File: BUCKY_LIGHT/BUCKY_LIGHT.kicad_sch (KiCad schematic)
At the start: 170 parts, among them Q1 Q_Photo_NPN, Q10 Q_Photo_NPN, Q11 Q_Photo_NPN, Q12 Q_Photo_NPN, Q13 Q_Photo_NPN, Q14 Q_Photo_NPN, Q15 Q_Photo_NPN, Q16 Q_Photo_NPN, Q17 Q_Photo_NPN, Q18 Q_Photo_NPN, Q19 Q_Photo_NPN, Q2 Q_Photo_NPN, Q20 Q_Photo_NPN, Q21 Q_Photo_NPN, Q22 Q_Photo_NPN, Q23 Q_Photo_NPN, Q24 Q_Photo_NPN, Q25 Q_Photo_NPN, Q26 Q_Photo_NPN, Q27 Q_Photo_NPN, Q28 Q_Photo_NPN, Q29 Q_Photo_NPN, Q3 Q_Photo_NPN, Q30 Q_Photo_NPN, Q31 Q_Photo_NPN, Q32 Q_Photo_NPN, Q4 Q_Photo_NPN, Q5 Q_Photo_NPN, Q6 Q_Photo_NPN, Q7 Q_Photo_NPN, Q8 Q_Photo_NPN, Q9 Q_Photo_NPN, U1 FRONT, U2 RIGHT, U3 DOWN, U4 LEFT

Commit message: Started Light PCB
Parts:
- removed C29, C30, C31, C32: 0.1u, Capacitor_SMD:C_0603_1608Metric_Pad1.08x0.95mm_HandSolder, symbol Device:C
- removed D29, D30, D31, D32: LED, LED_SMD:LED_0603_1608Metric, symbol Device:LED
- removed Q29, Q30, Q31, Q32: Q_Photo_NPN, Light_Ring:XDCR_ALS-PT19-315C_L177_TR8, symbol Device:Q_Photo_NPN
- removed R57, R58, R59, R60: 10k, Resistor_SMD:R_0603_1608Metric_Pad0.98x0.95mm_HandSolder, symbol Device:R
- removed R61, R62, R63, R64: 12R, Resistor_SMD:R_0603_1608Metric_Pad0.98x0.95mm_HandSolder, symbol Device:R
- C1, C10, C11, C12, C13, C14, C15, C16, C17, C18, C19, C2, C20, C21, C22, C23, C24, C25, C26, C27, C28, C3, C4, C5, C6, C7, C8, C9: footprint Capacitor_SMD:C_0603_1608Metric_Pad1.08x0.95mm_HandSolder -> Capacitor_SMD:C_0805_2012Metric_Pad1.18x1.45mm_HandSolder
- D1, D10, D11, D12, D13, D14, D15, D16, D17, D18, D19, D2, D20, D21, D22, D23, D24, D25, D26, D27, D28, D3, D4, D5, D6, D7, D8, D9: footprint LED_SMD:LED_0603_1608Metric -> LED_SMD:LED_PLCC-2
- J1: renamed from J?; footprint (none) -> Connector_JST:JST_PH_B6B-PH-SM4-TB_1x06-1MP_P2.00mm_Vertical
- J2: renamed from J?; footprint (none) -> Connector_JST:JST_PH_S6B-PH-SM4-TB_1x06-1MP_P2.00mm_Horizontal
- Q1, Q10, Q11, Q12, Q13, Q14, Q15, Q16, Q17, Q18, Q19, Q2, Q20, Q21, Q22, Q23, Q24, Q25, Q26, Q27, Q28, Q3, Q4, Q5, Q6, Q7, Q8, Q9: footprint Light_Ring:XDCR_ALS-PT19-315C_L177_TR8 -> BUCKY_LIGHT:XDCR_ALS-PT19-315C_L177_TR8
- R1, R10, R11, R12, R17, R18, R19, R2, R20, R25, R26, R27, R28, R3, R33, R34, R35, R36, R4, R41, R42, R43, R44, R49, R50, R51, R52, R9: footprint Resistor_SMD:R_0603_1608Metric_Pad0.98x0.95mm_HandSolder -> Resistor_SMD:R_0603_1608Metric
- R13, R14, R15, R16, R21, R22, R23, R24, R29, R30, R31, R32, R37, R38, R39, R40, R45, R46, R47, R48, R5, R53, R54, R55, R56, R6, R7, R8: value 12R -> 90R; footprint Resistor_SMD:R_0603_1608Metric_Pad0.98x0.95mm_HandSolder -> Resistor_SMD:R_0603_1608Metric
- R65, R66: renamed from R?; footprint (none) -> Resistor_SMD:R_0805_2012Metric_Pad1.20x1.40mm_HandSolder
- U1, U2, U3, U4: footprint (none) -> Package_SO:SOIC-16_3.9x9.9mm_P1.27mm
- U6: renamed from U?; value ESP32-WROOM-32D -> ESP32-WROOM-32U; footprint RF_Module:ESP32-WROOM-32 -> RF_Module:ESP32-WROOM-32U; symbol RF_Module:ESP32-WROOM-32D -> RF_Module:ESP32-WROOM-32U
- gave numbers to parts that had none: 1
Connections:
- net L29 is gone; now on net L26: U1.13 (A0)
- net L30 is gone; now on net L27: U1.14 (A1)
- net L31 is gone; now on net L28: U1.15 (A2)
- net L32 is gone; now on net L1: U1.12 (A3)
- net L1: no longer U1.1 (A4)
- net L12: now also U3.13 (A0); no longer U2.4 (A7)
- net L13: now also U3.14 (A1); no longer U3.13 (A0)
- net L14: now also U3.15 (A2); no longer U3.14 (A1)
- net L15: now also U3.12 (A3); no longer U3.15 (A2)
- net L16: now also U3.1 (A4); no longer U3.12 (A3)
- net L17: now also U3.5 (A5); no longer U3.1 (A4)
- net L18: now also U3.2 (A6); no longer U3.5 (A5)
- net L19: now also U4.13 (A0); no longer U3.2 (A6)
- net L2: now also U1.1 (A4); no longer U1.5 (A5)
- net L20: now also U4.14 (A1); no longer U3.4 (A7)
- net L21: now also U4.15 (A2); no longer U4.13 (A0)
- net L22: now also U4.12 (A3); no longer U4.14 (A1)
- net L23: now also U4.1 (A4); no longer U4.15 (A2)
- net L24: now also U4.5 (A5); no longer U4.12 (A3)
- net L25: now also U4.2 (A6); no longer U4.1 (A4)
- net L26: no longer U4.5 (A5)
- net L27: no longer U4.2 (A6)
- net L28: no longer U4.4 (A7)
- net L3: now also U1.5 (A5); no longer U1.2 (A6)
- net L4: now also U1.2 (A6); no longer U1.4 (A7)
- no-connect marks 12 -> 16
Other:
- note added: "IF Vf = 3.1V, then Rled = 90R IF Vf = 2.9V, then Rled = 25R"
- note removed: "IF Vf = 3.1V, then Rled = 12R IF Vf = 2.9V, then Rled = 25R"

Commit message: Some LIGHT dev
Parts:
- removed C10, C11, C12, C13, C14, C15, C16, C17, C18, C19, C20, C21, C22, C23, C24, C25, C26, C27, C28, C5, C6, C7, C8, C9: 0.1u, Capacitor_SMD:C_0805_2012Metric_Pad1.18x1.45mm_HandSolder, symbol Device:C
- added U7: AMS1117-3.3, Package_TO_SOT_SMD:SOT-223-3_TabPin2, symbol Regulator_Linear:AMS1117-3.3
- C1: value 0.1u -> 22u; footprint Capacitor_SMD:C_0805_2012Metric_Pad1.18x1.45mm_HandSolder -> Capacitor_SMD:C_1210_3225Metric_Pad1.33x2.70mm_HandSolder
- C2, C4: footprint Capacitor_SMD:C_0805_2012Metric_Pad1.18x1.45mm_HandSolder -> Capacitor_SMD:C_1210_3225Metric_Pad1.33x2.70mm_HandSolder
- C3: value 0.1u -> 10u; footprint Capacitor_SMD:C_0805_2012Metric_Pad1.18x1.45mm_HandSolder -> Capacitor_SMD:C_1210_3225Metric_Pad1.33x2.70mm_HandSolder
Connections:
- net +3V3: now also C3.1, C4.1, U7.2 (VO); no longer R13.1, R14.1, R15.1, R16.1, R21.1, R22.1, R23.1, R24.1, R29.1, R30.1, R31.1, R32.1, R37.1, R38.1, R39.1, R40.1, R45.1, R46.1, R47.1, R48.1, R5.1, R53.1, R54.1, R55.1, R56.1, R6.1, R7.1, R8.1
- net +5V: now also C1.1, C2.1, R13.1, R14.1, R15.1, R16.1, R21.1, R22.1, R23.1, R24.1, R29.1, R30.1, R31.1, R32.1, R37.1, R38.1, R39.1, R40.1, R45.1, R46.1, R47.1, R48.1, R5.1, R53.1, R54.1, R6.1, R7.1, R8.1, U7.3 (VI)
- net GND: now also U7.1 (GND)
- net L1: no longer C1.1
- net L2: no longer C2.1
- net L3: no longer C3.1
- net L4: no longer C4.1

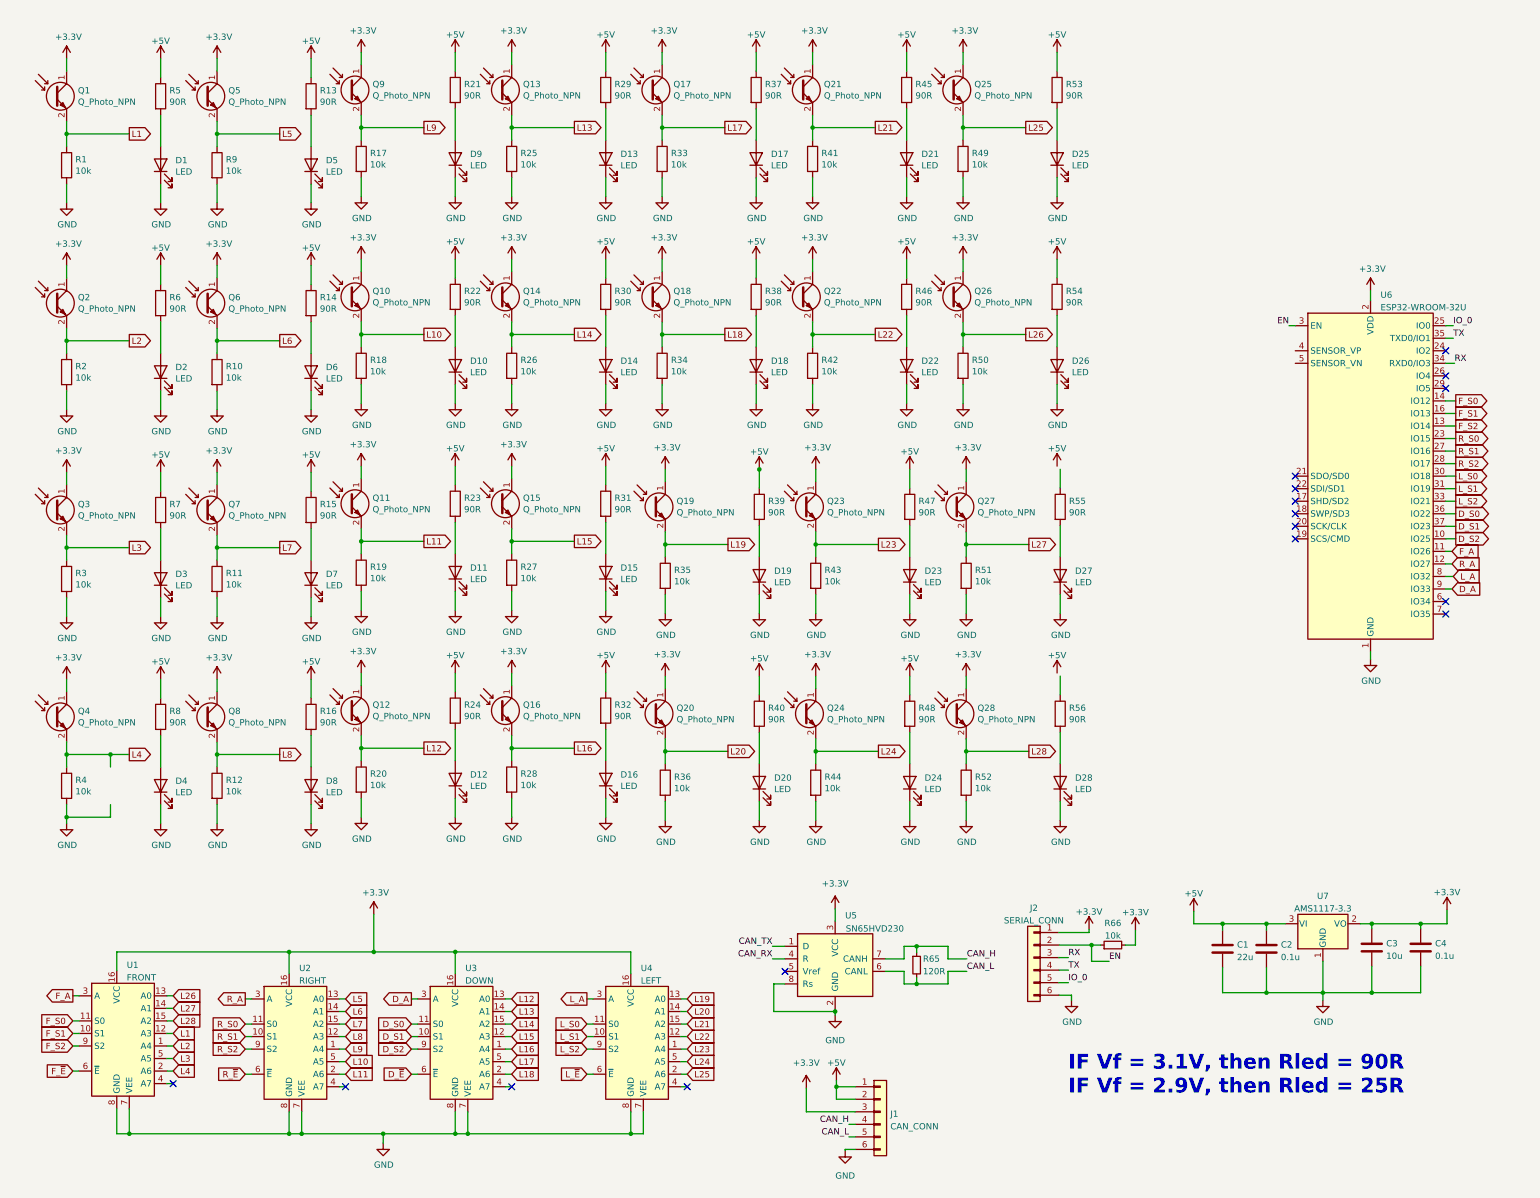
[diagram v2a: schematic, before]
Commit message: Finished bulk of LIGHT, only REF left
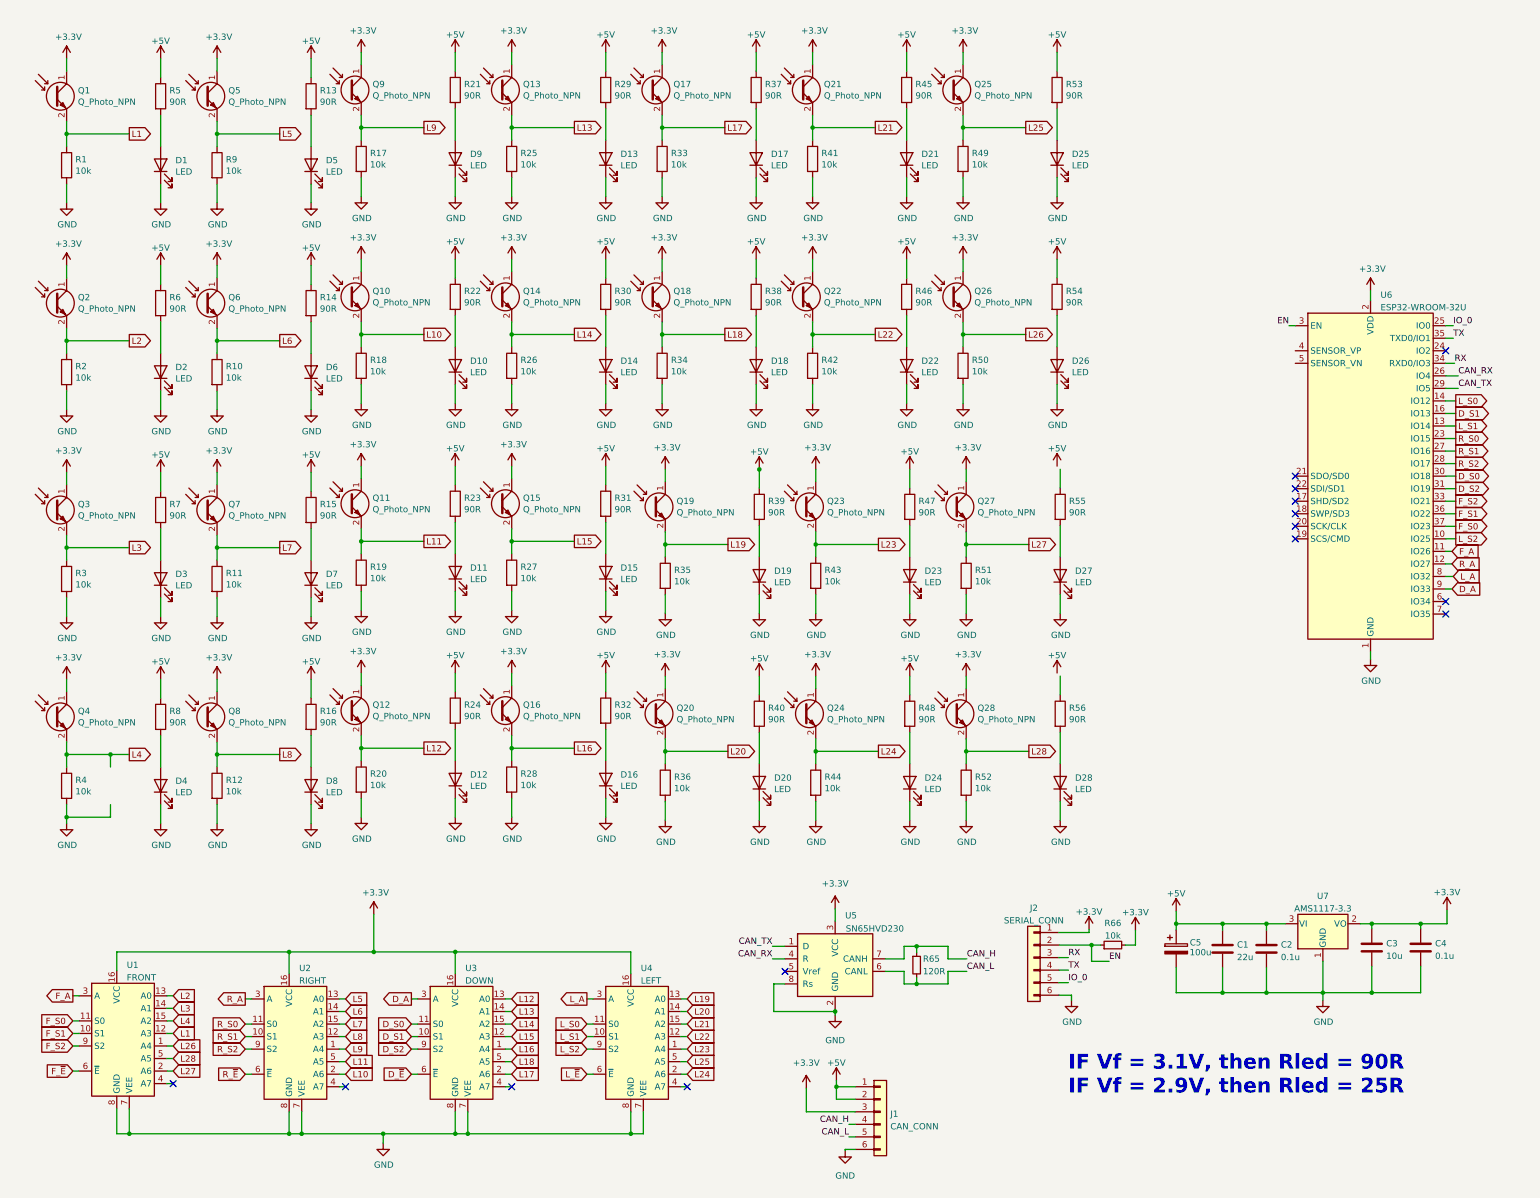
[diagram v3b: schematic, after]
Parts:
- added C5: 100u, Capacitor_SMD:CP_Elec_6.3x7.7, symbol Device:C_Polarized
- C2, C4: footprint Capacitor_SMD:C_1210_3225Metric_Pad1.33x2.70mm_HandSolder -> Capacitor_SMD:C_0603_1608Metric
- J2: footprint Connector_JST:JST_PH_S6B-PH-SM4-TB_1x06-1MP_P2.00mm_Horizontal -> Connector_JST:JST_PH_B6B-PH-SM4-TB_1x06-1MP_P2.00mm_Vertical
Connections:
- net +5V: now also C5.1
- net CAN_RX: now also U6.26 (IO4)
- net CAN_TX: now also U6.29 (IO5)
- net D_S0: now also U6.30 (IO18); no longer U6.36 (IO22)
- net D_S1: now also U6.16 (IO13); no longer U6.37 (IO23)
- net D_S2: now also U6.31 (IO19); no longer U6.10 (IO25)
- net F_S0: now also U6.37 (IO23); no longer U6.14 (IO12)
- net F_S1: now also U6.36 (IO22); no longer U6.16 (IO13)
- net F_S2: now also U6.33 (IO21); no longer U6.13 (IO14)
- net GND: now also C5.2
- net L10: now also U2.2 (A6); no longer U2.5 (A5)
- net L11: now also U2.5 (A5); no longer U2.2 (A6)
- net L17: now also U3.2 (A6); no longer U3.5 (A5)
- net L18: now also U3.5 (A5); no longer U3.2 (A6)
- net L2: now also U1.13 (A0); no longer U1.1 (A4)
- net L24: now also U4.2 (A6); no longer U4.5 (A5)
- net L25: now also U4.5 (A5); no longer U4.2 (A6)
- net L26: now also U1.1 (A4); no longer U1.13 (A0)
- net L27: now also U1.2 (A6); no longer U1.14 (A1)
- net L28: now also U1.5 (A5); no longer U1.15 (A2)
- net L3: now also U1.14 (A1); no longer U1.5 (A5)
- net L4: now also U1.15 (A2); no longer U1.2 (A6)
- net L_S0: now also U6.14 (IO12); no longer U6.30 (IO18)
- net L_S1: now also U6.13 (IO14); no longer U6.31 (IO19)
- net L_S2: now also U6.10 (IO25); no longer U6.33 (IO21)
- no-connect marks 16 -> 14

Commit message: Started POWER
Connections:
- net +5V: now also R55.1, R56.1
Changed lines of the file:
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@@
     (pin "2")
   )
-  (symbol (lib_id "power:+5V") (at 222.25 143.51 0) (unit 1)
-    (in_bom yes) (on_board yes) (fields_autoplaced)
-    (property "Reference" "#PWR0111" (id 0) (at 222.25 147.32 0)
-      (effects (font (size 1.27 1.27)) hide)
-    )
-    (property "Value" "+5V" (id 1) (at 222.25 139.9342 0))
-    (property "Footprint" "" (id 2) (at 222.25 143.51 0)
-      (effects (font (size 1.27 1.27)) hide)
-    )
-    (property "Datasheet" "" (id 3) (at 222.25 143.51 0)
+  (symbol (lib_id "power:+5V") (at 222.885 144.145 0) (unit 1)
+    (in_bom yes) (on_board yes) (fields_autoplaced)
+    (property "Reference" "#PWR0111" (id 0) (at 222.885 147.955 0)
+      (effects (font (size 1.27 1.27)) hide)
+    )
+    (property "Value" "+5V" (id 1) (at 222.885 140.5692 0))
+    (property "Footprint" "" (id 2) (at 222.885 144.145 0)
+      (effects (font (size 1.27 1.27)) hide)
+    )
+    (property "Datasheet" "" (id 3) (at 222.885 144.145 0)
       (effects (font (size 1.27 1.27)) hide)
     )
@@
     (pin "2")
   )
-  (symbol (lib_id "power:+5V") (at 222.25 101.6 0) (unit 1)
-    (in_bom yes) (on_board yes) (fields_autoplaced)
-    (property "Reference" "#PWR0153" (id 0) (at 222.25 105.41 0)
-      (effects (font (size 1.27 1.27)) hide)
-    )
-    (property "Value" "+5V" (id 1) (at 222.25 98.0242 0))
-    (property "Footprint" "" (id 2) (at 222.25 101.6 0)
-      (effects (font (size 1.27 1.27)) hide)
-    )
-    (property "Datasheet" "" (id 3) (at 222.25 101.6 0)
-      (effects (font (size 1.27 1.27)) hide)
-    )
+  (symbol (lib_id "power:+5V") (at 222.885 102.235 0) (unit 1)
+    (in_bom yes) (on_board yes) (fields_autoplaced)
+    (property "Reference" "#PWR0153" (id 0) (at 222.885 106.045 0)
+      (effects (font (size 1.27 1.27)) hide)
+    )
+    (property "Value" "+5V" (id 1) (at 222.885 98.6592 0))
+    (property "Footprint" "" (id 2) (at 222.885 102.235 0)
+      (effects (font (size 1.27 1.27)) hide)
+    )
+    (property "Datasheet" "" (id 3) (at 222.885 102.235 0)
+      (effects (font (size 1.27 1.27)) hide)
+    )

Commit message: chore: start on schematics
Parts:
- removed C1: 22u, Capacitor_SMD:C_1210_3225Metric_Pad1.33x2.70mm_HandSolder, symbol Device:C
- removed C2, C4: 0.1u, Capacitor_SMD:C_0603_1608Metric, symbol Device:C
- removed C3: 10u, Capacitor_SMD:C_1210_3225Metric_Pad1.33x2.70mm_HandSolder, symbol Device:C
- removed C5: 100u, Capacitor_SMD:CP_Elec_6.3x7.7, symbol Device:C_Polarized
- removed J1: CAN_CONN, Connector_JST:JST_PH_B6B-PH-SM4-TB_1x06-1MP_P2.00mm_Vertical, symbol Connector_Generic:Conn_01x06
- removed J2: SERIAL_CONN, Connector_JST:JST_PH_B6B-PH-SM4-TB_1x06-1MP_P2.00mm_Vertical, symbol Connector_Generic:Conn_01x06
- removed R65: 120R, Resistor_SMD:R_0805_2012Metric_Pad1.20x1.40mm_HandSolder, symbol Device:R_Small
- removed R66: 10k, Resistor_SMD:R_0805_2012Metric_Pad1.20x1.40mm_HandSolder, symbol Device:R_Small
- removed U5: SN65HVD230, Package_SO:SOIC-8_3.9x4.9mm_P1.27mm, symbol Interface_CAN_LIN:SN65HVD230
- removed U6: ESP32-WROOM-32U, RF_Module:ESP32-WROOM-32U, symbol RF_Module:ESP32-WROOM-32U
- removed U7: AMS1117-3.3, Package_TO_SOT_SMD:SOT-223-3_TabPin2, symbol Regulator_Linear:AMS1117-3.3
- added J1: Conn_01x16, BUCKY_LIGHT:BUCKY_LIGHT_POWER, symbol Connector_Generic:Conn_01x16
- added J2: Conn_01x02, BUCKY_LIGHT:BUCKY_POWER_CONN, symbol Connector_Generic:Conn_01x02
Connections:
- net +3V3 is gone; now on net +5V: Q1.1 (C), Q10.1 (C), Q11.1 (C), Q12.1 (C), Q13.1 (C), Q14.1 (C), Q15.1 (C), Q16.1 (C), Q17.1 (C), Q18.1 (C), Q19.1 (C), Q2.1 (C), Q20.1 (C), Q21.1 (C), Q22.1 (C), Q23.1 (C), Q24.1 (C), Q25.1 (C), Q26.1 (C), Q27.1 (C), Q28.1 (C), Q3.1 (C), Q4.1 (C), Q5.1 (C), Q6.1 (C), Q7.1 (C), Q8.1 (C), Q9.1 (C), U1.16 (VCC), U2.16 (VCC), U3.16 (VCC), U4.16 (VCC)
- net +5V: now also J2.1 (Pin_1)
- net D_A: now also J1.10 (Pin_10)
- net D_S0: now also J1.7 (Pin_7)
- net D_S1: now also J1.9 (Pin_9)
- net D_S2: now also J1.8 (Pin_8)
- net F_A: now also J1.12 (Pin_12)
- net F_S0: now also J1.11 (Pin_11)
- net F_S1: now also J1.6 (Pin_6)
- net F_S2: now also J1.5 (Pin_5)
- net GND: now also J2.2 (Pin_2)
- net L_A: now also J1.13 (Pin_13)
- net L_S0: now also J1.16 (Pin_16)
- net L_S1: now also J1.15 (Pin_15)
- net L_S2: now also J1.14 (Pin_14)
- net R_A: now also J1.1 (Pin_1)
- net R_S0: now also J1.2 (Pin_2)
- net R_S1: now also J1.3 (Pin_3)
- net R_S2: now also J1.4 (Pin_4)
- no-connect marks 14 -> 4
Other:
- note added: "CONNECTORS (TO BUCKY IR)"
- note added: "LIGHT SENSORS"
- note added: "LIGHT SENSORS ANALOG PIN MULTIPLEXER"
- note removed: "IF Vf = 3.1V, then Rled = 90R IF Vf = 2.9V, then Rled = 25R"
- company: (none) -> koen1711
- title: (none) -> BUCKY LIGHT
- moved on the sheet: D19, D20, D23, D24, D27, D28, Q19, Q20, Q23, Q24, Q27, Q28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

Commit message: chore: finish main board
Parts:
- removed J1: Conn_01x16, BUCKY_LIGHT:BUCKY_LIGHT_POWER, symbol Connector_Generic:Conn_01x16
- removed J2: Conn_01x02, BUCKY_LIGHT:BUCKY_POWER_CONN, symbol Connector_Generic:Conn_01x02
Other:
- added sheet CONNECTORS (CONN.kicad_sch)
- note added: "CD74HC4051"
- note removed: "CONNECTORS (TO BUCKY IR)"
